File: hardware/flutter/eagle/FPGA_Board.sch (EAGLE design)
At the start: 61 parts, among them IC1 AT45DB161D-SU, IC2 MEGA8-AI, IC3 MAX481CSA, Q1 8Mhz, U2 XC3S50AVQ100

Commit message: update of flutter: didn't know what i have done....
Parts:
- added R20: 10k, resistor:R-EU_M0805
- added X1: BU-SMA-V, con-coax:BU-SMA-V
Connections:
- new net GPS_NRESET: IC2.PD5(T1), R20.2, U$6.NRESET
- new net GPS_RX: IC2.PD7(AIN1), U$6.RXDA
- new net GPS_TX: IC2.PD6(AIN0), U$6.TXDA
- new net N$14: U$6.EX_ANT, X1G$1.1
- net GND: now also R20.1, U$6.GND1, U$6.GND2, U$6.GND3, U$6.GND4, U$6.RTCM, X1G$1.GND
- net PPS: now also U$6.1PPS
- net VCC3.3: now also U$6.VBACKUP, U$6.VCC
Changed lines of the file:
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@@
 <part name="IC3" library="maxim" deviceset="MAX481CSA" device=""/>
 <part name="U$6" library="hgg" deviceset="GPS" device=""/>
+<part name="R20" library="resistor" deviceset="R-EU_" device="M0805" value="10k"/>
+<part name="GND41" library="supply1" deviceset="GND" device=""/>
+<part name="GND42" library="supply1" deviceset="GND" device=""/>
+<part name="GND43" library="supply1" deviceset="GND" device=""/>
+<part name="GND44" library="supply1" deviceset="GND" device=""/>
+<part name="GND45" library="supply1" deviceset="GND" device=""/>
+<part name="GND46" library="supply1" deviceset="GND" device=""/>
+<part name="X1" library="con-coax" deviceset="BU-SMA-V" device=""/>
+<part name="GND47" library="supply1" deviceset="GND" device=""/>
 </parts>
 <sheets>
@@
 <instance part="IC3" gate="P" x="490.22" y="210.82"/>
 <instance part="U$6" gate="G$1" x="368.3" y="274.32"/>
+<instance part="R20" gate="G$1" x="332.74" y="287.02" rot="R90"/>
+<instance part="GND41" gate="1" x="332.74" y="279.4"/>
+<instance part="GND42" gate="1" x="340.36" y="287.02" rot="R270"/>
+<instance part="GND43" gate="1" x="340.36" y="261.62" rot="R270"/>
+<instance part="GND44" gate="1" x="396.24" y="256.54" rot="R90"/>
+<instance part="GND45" gate="1" x="396.24" y="292.1" rot="R90"/>
+<instance part="GND46" gate="1" x="396.24" y="266.7" rot="R90"/>
+<instance part="X1" gate="G$1" x="411.48" y="251.46" rot="R180"/>
+<instance part="GND47" gate="1" x="406.4" y="254" rot="R270"/>
 </instances>
 <busses>
@@
 <wire x1="233.68" y1="81.28" x2="259.08" y2="81.28" width="0.1524" layer="91"/>
 </segment>
+<segment>
+<pinref part="R20" gate="G$1" pin="1"/>
+<pinref part="GND41" gate="1" pin="GND"/>
+</segment>
+<segment>
+<pinref part="U$6" gate="G$1" pin="GND1"/>
+<pinref part="GND42" gate="1" pin="GND"/>
+</segment>
+<segment>
+<pinref part="U$6" gate="G$1" pin="GND2"/>
+<pinref part="GND43" gate="1" pin="GND"/>
+</segment>
+<segment>
+<pinref part="U$6" gate="G$1" pin="GND4"/>
+<pinref part="GND45" gate="1" pin="GND"/>
+</segment>
+<segment>
+<pinref part="U$6" gate="G$1" pin="GND3"/>
+<pinref part="GND44" gate="1" pin="GND"/>
+</segment>
+<segment>
+<pinref part="U$6" gate="G$1" pin="RTCM"/>
+<pinref part="GND46" gate="1" pin="GND"/>
+</segment>
+<segment>
+<pinref part="X1" gate="G$1" pin="GND"/>
+<pinref part="GND47" gate="1" pin="GND"/>
+</segment>
 </net>
 <net name="+5V" class="0">
@@
 <wire x1="378.46" y1="195.58" x2="360.68" y2="195.58" width="0.1524" layer="91"/>
 <label x="360.68" y="195.58" size="1.778" layer="95"/>
+</segment>
+<segment>
+<pinref part="U$6" gate="G$1" pin="VCC"/>
+<wire x1="342.9" y1="297.18" x2="335.28" y2="297.18" width="0.1524" layer="91"/>
+<wire x1="335.28" y1="297.18" x2="335.28" y2="304.8" width="0.1524" layer="91"/>
+<label x="335.28" y="302.26" size="1.778" layer="95"/>
+<pinref part="U$6" gate="G$1" pin="VBACKUP"/>
+<wire x1="342.9" y1="281.94" x2="335.28" y2="281.94" width="0.1524" layer="91"/>
+<wire x1="335.28" y1="281.94" x2="335.28" y2="297.18" width="0.1524" layer="91"/>
+<junction x="335.28" y="297.18"/>
 </segment>
 </net>
@@
 <label x="66.04" y="264.16" size="1.778" layer="95"/>
 </segment>
+<segment>
+<pinref part="U$6" gate="G$1" pin="1PPS"/>
+<wire x1="393.7" y1="261.62" x2="411.48" y2="261.62" width="0.1524" layer="91"/>
+<label x="406.4" y="261.62" size="1.778" layer="95"/>
+</segment>
 </net>
 <net name="FASTCLK+" class="0">
@@
 </segment>
 </net>
+<net name="GPS_NRESET" class="0">
+<segment>
+<pinref part="U$6" gate="G$1" pin="NRESET"/>
+<wire x1="342.9" y1="292.1" x2="332.74" y2="292.1" width="0.1524" layer="91"/>
+<pinref part="R20" gate="G$1" pin="2"/>
+<wire x1="332.74" y1="292.1" x2="325.12" y2="292.1" width="0.1524" layer="91"/>
+<label x="325.12" y="292.1" size="1.778" layer="95"/>
+</segment>
+<segment>
+<pinref part="IC2" gate="G$1" pin="PD5(T1)"/>
+<wire x1="426.72" y1="170.18" x2="454.66" y2="170.18" width="0.1524" layer="91"/>
+<label x="447.04" y="170.18" size="1.778" layer="95"/>
+</segment>
+</net>
+<net name="GPS_TX" class="0">
+<segment>
+<pinref part="U$6" gate="G$1" pin="TXDA"/>
+<wire x1="342.9" y1="256.54" x2="327.66" y2="256.54" width="0.1524" layer="91"/>
+<label x="327.66" y="256.54" size="1.778" layer="95"/>
+</segment>
+<segment>
+<pinref part="IC2" gate="G$1" pin="PD6(AIN0)"/>
+<wire x1="426.72" y1="167.64" x2="454.66" y2="167.64" width="0.1524" layer="91"/>
+<label x="447.04" y="167.64" size="1.778" layer="95"/>
+</segment>
+</net>
+<net name="GPS_RX" class="0">
+<segment>
+<pinref part="U$6" gate="G$1" pin="RXDA"/>
+<wire x1="342.9" y1="251.46" x2="327.66" y2="251.46" width="0.1524" layer="91"/>
+<label x="327.66" y="251.46" size="1.778" layer="95"/>
+</segment>
+<segment>
+<pinref part="IC2" gate="G$1" pin="PD7(AIN1)"/>
+<wire x1="426.72" y1="165.1" x2="454.66" y2="165.1" width="0.1524" layer="91"/>
+<label x="447.04" y="165.1" size="1.778" layer="95"/>
+</segment>
+</net>
+<net name="N$14" class="0">
+<segment>
+<pinref part="X1" gate="G$1" pin="1"/>
+<pinref part="U$6" gate="G$1" pin="EX_ANT"/>
+<wire x1="408.94" y1="251.46" x2="393.7" y2="251.46" width="0.1524" layer="91"/>
+</segment>
+</net>

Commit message: Added testpoints
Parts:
- removed R16: 1k, resistor:R-EU_M0805
- removed R17: 1.6k, resistor:R-EU_M0805
- added TP1, TP10, TP11, TP12, TP13, TP14, TP15, TP16, TP17, TP18, TP2, TP3, TP4, TP5, TP6, TP7, TP8, TP9: TPB2,54, testpad:TPB2,54
- added X2: MINI-USB-32005-201, con-cypressindustries:MINI-USB-32005-201
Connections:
- net N$6 renamed DI
- removed net N$10: IC3G$1.RO, R16.2
- removed net N$9: IC2.PD0(RXD), R16.1, R17.2
- new net CS: IC2.PD2(INT0), U$4./CS,IRQ
- new net D+: U$6.DPLUSE, X2.3
- new net D-: U$6.DMINUS, X2.2
- new net DO: IC2.PD0(RXD), IC3G$1.RO
- new net IRQ: IC2.PB0(ICP), U$4.IRQ
- new net N$15: X2.4
- new net TIMING_CLK: QG1.OUT, TP8.TP, U2B0.IO_L02N_0/GCLK5
- new net USBVCC: U$6.USB-VCC, X2.1
- net +5V: now also TP1.TP; no longer IC3P.VCC
- net FASTCLK+: now also TP6.TP, U2B3.IO_L03P_3/LHCLK0
- net FASTCLK-: now also TP7.TP, U2B3.IO_L03N_3/LHCLK1
- net FPGA_SPI_CLOCK: now also TP9.TP; no longer QG1.OUT
- net GND: now also X2.5; no longer R17.1
- net GPS_NRESET: now also TP12.TP
- net GPS_RX: now also TP11.TP
- net GPS_TX: now also TP10.TP
- net N$5: now also IC2.PD4(XCK/T0); no longer IC2.PD2(INT0)
- net PPS: now also IC2.PD3(INT1), TP5.TP
- net SLOWCLK/CLK: now also TP13.TP
- net SLOWCLK/CS: now also TP14.TP
- net SLOWCLK/MOSI: now also TP15.TP
- net UC_FPGA_SPI_CS: now also TP17.TP
- net UC_MOSI: now also TP18.TP
- net UC_SCK: now also TP16.TP
- net VCC1.2: now also TP4.TP
- net VCC2.5: now also TP3.TP
- net VCC3.3: now also IC3P.VCC, TP2.TP

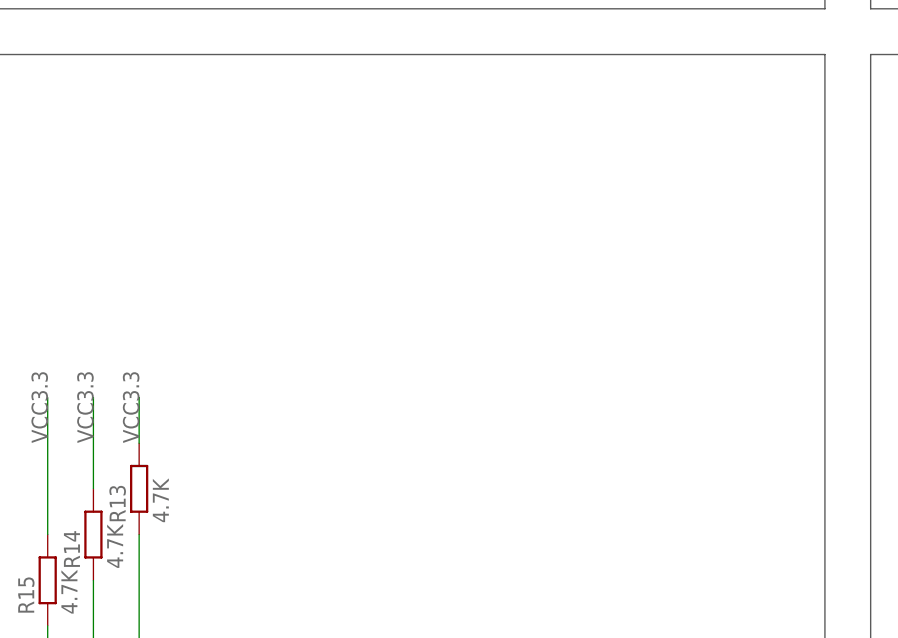
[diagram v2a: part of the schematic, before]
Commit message: added pinheader to access fpga's eeprom pins
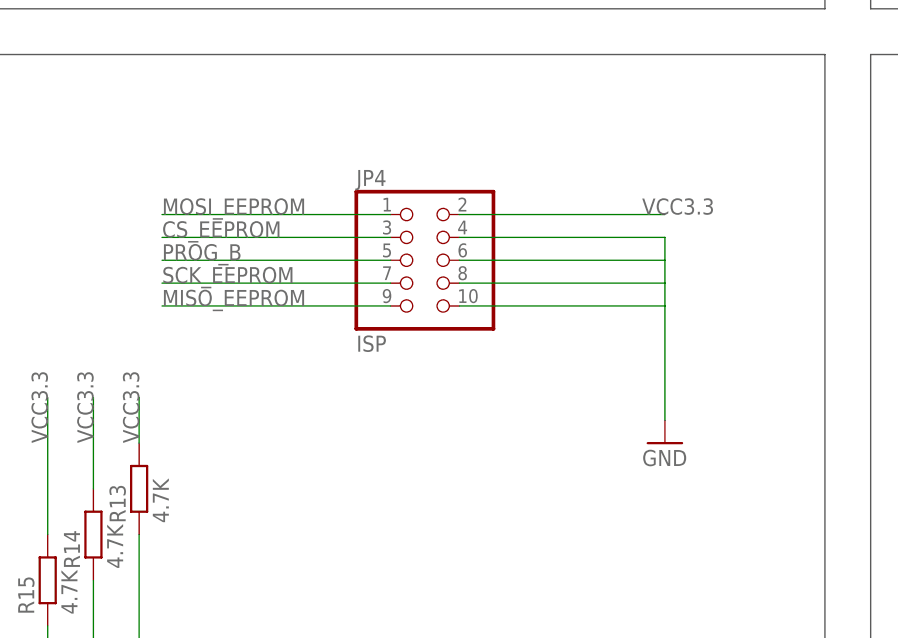
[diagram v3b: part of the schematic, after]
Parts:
- added JP4: ISP, pinhead:PINHD-2X5
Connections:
- net CS_EEPROM: now also JP4.3
- net GND: now also JP4.10, JP4.4, JP4.6, JP4.8
- net MISO_EEPROM: now also JP4.9
- net MOSI_EEPROM: now also JP4.1
- net PROG_B: now also JP4.5
- net SCK_EEPROM: now also JP4.7
- net VCC3.3: now also JP4.2
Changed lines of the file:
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@@
 <part name="TP17" library="testpad" deviceset="TP" device="B2,54"/>
 <part name="TP18" library="testpad" deviceset="TP" device="B2,54"/>
+<part name="JP4" library="pinhead" deviceset="PINHD-2X5" device="" value="ISP"/>
+<part name="GND26" library="supply1" deviceset="GND" device=""/>
 </parts>
 <sheets>
@@
 <instance part="TP17" gate="G$1" x="254" y="347.98"/>
 <instance part="TP18" gate="G$1" x="261.62" y="347.98"/>
+<instance part="JP4" gate="A" x="271.78" y="208.28"/>
+<instance part="GND26" gate="1" x="299.72" y="187.96"/>
 </instances>
 <busses>
@@
 <label x="411.48" y="276.86" size="1.778" layer="95"/>
 </segment>
+<segment>
+<pinref part="JP4" gate="A" pin="4"/>
+<wire x1="276.86" y1="210.82" x2="299.72" y2="210.82" width="0.1524" layer="91"/>
+<wire x1="299.72" y1="210.82" x2="299.72" y2="208.28" width="0.1524" layer="91"/>
+<pinref part="JP4" gate="A" pin="8"/>
+<wire x1="299.72" y1="208.28" x2="299.72" y2="205.74" width="0.1524" layer="91"/>
+<wire x1="299.72" y1="205.74" x2="276.86" y2="205.74" width="0.1524" layer="91"/>
+<pinref part="JP4" gate="A" pin="6"/>
+<wire x1="276.86" y1="208.28" x2="299.72" y2="208.28" width="0.1524" layer="91"/>
+<pinref part="JP4" gate="A" pin="10"/>
+<wire x1="276.86" y1="203.2" x2="299.72" y2="203.2" width="0.1524" layer="91"/>
+<wire x1="299.72" y1="203.2" x2="299.72" y2="205.74" width="0.1524" layer="91"/>
+<wire x1="299.72" y1="203.2" x2="299.72" y2="190.5" width="0.1524" layer="91"/>
+<pinref part="GND26" gate="1" pin="GND"/>
+</segment>
 </net>
 <net name="+5V" class="0">
@@
 <wire x1="139.7" y1="345.44" x2="139.7" y2="322.58" width="0.1524" layer="91"/>
 <label x="139.7" y="322.58" size="1.778" layer="95" rot="R90"/>
+</segment>
+<segment>
+<pinref part="JP4" gate="A" pin="2"/>
+<wire x1="276.86" y1="213.36" x2="299.72" y2="213.36" width="0.1524" layer="91"/>
+<label x="297.18" y="213.36" size="1.778" layer="95"/>
 </segment>
 </net>
@@
 <pinref part="R12" gate="G$1" pin="1"/>
 </segment>
+<segment>
+<pinref part="JP4" gate="A" pin="5"/>
+<wire x1="269.24" y1="208.28" x2="243.84" y2="208.28" width="0.1524" layer="91"/>
+<label x="243.84" y="208.28" size="1.778" layer="95"/>
+</segment>
 </net>
 <net name="FPGA_SPI_CLOCK" class="0">
@@
 <wire x1="157.48" y1="154.94" x2="190.5" y2="154.94" width="0.1524" layer="91"/>
 <label x="182.88" y="154.94" size="1.778" layer="95"/>
+</segment>
+<segment>
+<pinref part="JP4" gate="A" pin="9"/>
+<wire x1="269.24" y1="203.2" x2="243.84" y2="203.2" width="0.1524" layer="91"/>
+<label x="243.84" y="203.2" size="1.778" layer="95"/>
 </segment>
 </net>
@@
 <label x="182.88" y="200.66" size="1.778" layer="95"/>
 </segment>
+<segment>
+<pinref part="JP4" gate="A" pin="3"/>
+<wire x1="269.24" y1="210.82" x2="243.84" y2="210.82" width="0.1524" layer="91"/>
+<label x="243.84" y="210.82" size="1.778" layer="95"/>
+</segment>
 </net>
 <net name="SCK_EEPROM" class="0">
@@
 <wire x1="157.48" y1="149.86" x2="190.5" y2="149.86" width="0.1524" layer="91"/>
 <label x="182.88" y="149.86" size="1.778" layer="95"/>
+</segment>
+<segment>
+<pinref part="JP4" gate="A" pin="7"/>
+<wire x1="269.24" y1="205.74" x2="243.84" y2="205.74" width="0.1524" layer="91"/>
+<label x="243.84" y="205.74" size="1.778" layer="95"/>
 </segment>
 </net>
@@
 <label x="182.88" y="210.82" size="1.778" layer="95"/>
 </segment>
-</net>
+<segment>
+<pinref part="JP4" gate="A" pin="1"/>
+<wire x1="269.24" y1="213.36" x2="243.84" y2="213.36" width="0.1524" layer="91"/>
+<label x="243.84" y="213.36" size="1.778" layer="95"/>
+</segment>
+</net>

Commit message: testpads are 20% cooler now!
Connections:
- removed net FASTCLK3V3: U$4.FASTCLK3V3
- net FASTCLK+: now also U$4.FASTCLK3V3
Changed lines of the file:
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@@
 <label x="170.18" y="322.58" size="1.778" layer="95" rot="R90"/>
+</segment>
+<segment>
+<pinref part="U$4" gate="G$1" pin="FASTCLK3V3"/>
+<wire x1="172.72" y1="15.24" x2="134.62" y2="15.24" width="0.1524" layer="91"/>
+<label x="134.62" y="15.24" size="1.778" layer="95"/>
 </segment>
 </net>
@@
 </segment>
 </net>
-<net name="FASTCLK3V3" class="0">
-<segment>
-<pinref part="U$4" gate="G$1" pin="FASTCLK3V3"/>
-<wire x1="172.72" y1="15.24" x2="134.62" y2="15.24" width="0.1524" layer="91"/>
-<label x="134.62" y="15.24" size="1.778" layer="95"/>
-</segment>
-</net>
